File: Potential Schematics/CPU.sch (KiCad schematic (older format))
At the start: 0 parts

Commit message: Made the registers
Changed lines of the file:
@@
 $Descr A4 11693 8268
 encoding utf-8
-Sheet 2 22
+Sheet 2 449
 Title "CPU"
-Date ""
+Date "2018-09-14"
 Rev "1"
 Comp ""
@@
 	2100 4000 2800 4000
 Connection ~ 2100 3400
+$Sheet
+S 6450 2150 1350 1300
+U 5B9C0EA0
+F0 "Registers" 60
+F1 "Registers.sch" 60
+$EndSheet
 $EndSCHEMATC

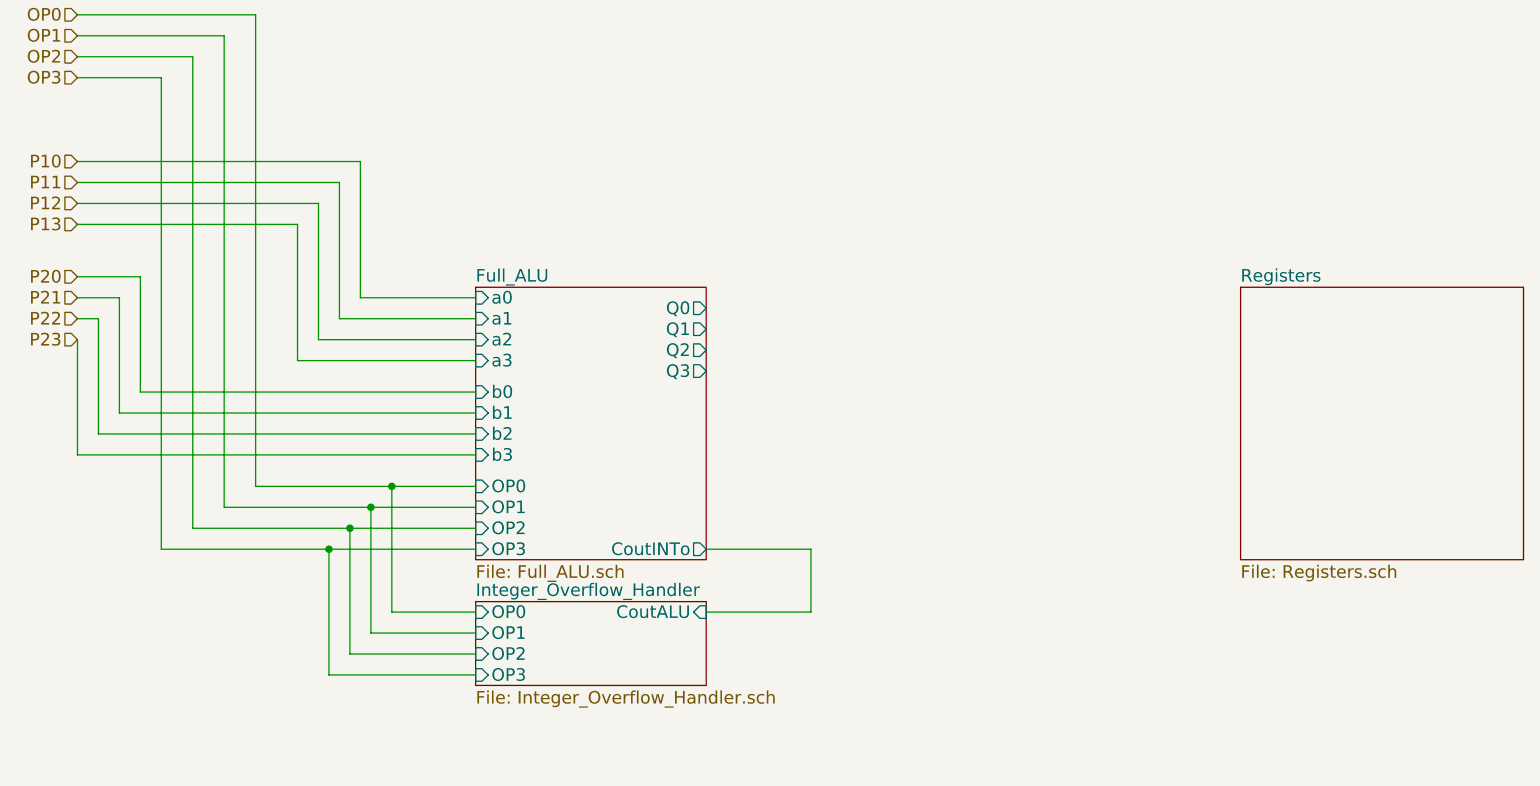
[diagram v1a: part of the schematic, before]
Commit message: Added Registers to Top Schematic
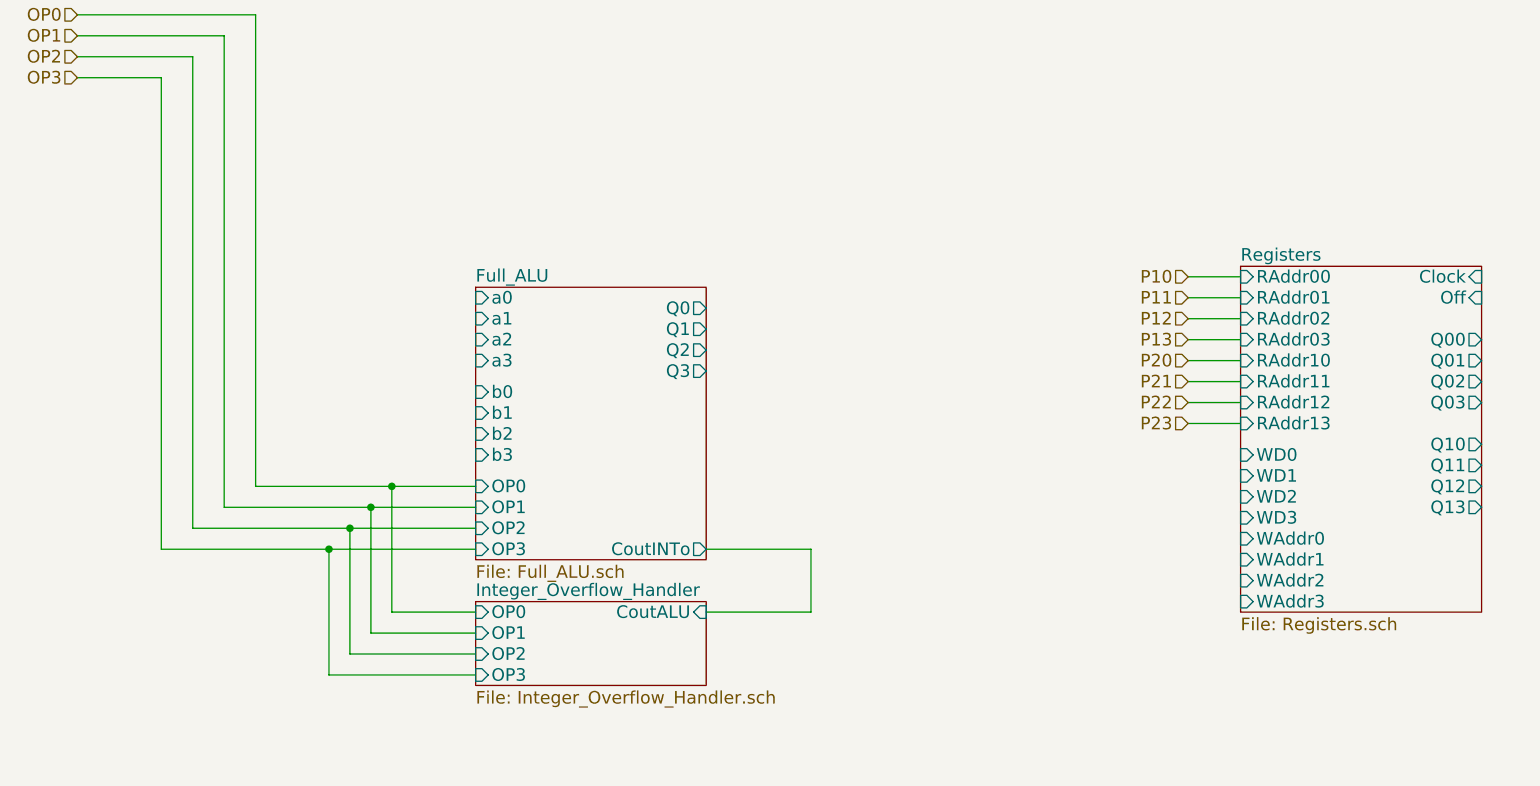
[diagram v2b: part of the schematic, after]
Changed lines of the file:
@@
 Text HLabel 900  1150 0    60   Input ~ 0
 OP3
-Text HLabel 900  1550 0    60   Input ~ 0
+Text HLabel 6200 2100 0    60   Input ~ 0
 P10
-Text HLabel 900  1650 0    60   Input ~ 0
+Text HLabel 6200 2200 0    60   Input ~ 0
 P11
-Text HLabel 900  1750 0    60   Input ~ 0
+Text HLabel 6200 2300 0    60   Input ~ 0
 P12
-Text HLabel 900  1850 0    60   Input ~ 0
+Text HLabel 6200 2400 0    60   Input ~ 0
 P13
-Text HLabel 900  2100 0    60   Input ~ 0
+Text HLabel 6200 2500 0    60   Input ~ 0
 P20
-Text HLabel 900  2200 0    60   Input ~ 0
+Text HLabel 6200 2600 0    60   Input ~ 0
 P21
-Text HLabel 900  2300 0    60   Input ~ 0
+Text HLabel 6200 2700 0    60   Input ~ 0
 P22
-Text HLabel 900  2400 0    60   Input ~ 0
+Text HLabel 6200 2800 0    60   Input ~ 0
 P23
 Text HLabel 900  4700 0    60   Input ~ 0
@@
 Wire Wire Line
 	1300 3400 2800 3400
-Wire Wire Line
-	900  1550 2250 1550
-Wire Wire Line
-	2250 1550 2250 2200
-Wire Wire Line
-	2250 2200 2800 2200
-Wire Wire Line
-	900  1650 2150 1650
-Wire Wire Line
-	2150 1650 2150 2300
-Wire Wire Line
-	2150 2300 2800 2300
-Wire Wire Line
-	2800 2400 2050 2400
-Wire Wire Line
-	2050 2400 2050 1750
-Wire Wire Line
-	2050 1750 900  1750
-Wire Wire Line
-	1950 2500 2800 2500
-Wire Wire Line
-	2800 2650 1200 2650
-Wire Wire Line
-	1200 2650 1200 2100
-Wire Wire Line
-	1200 2100 900  2100
-Wire Wire Line
-	900  2200 1100 2200
-Wire Wire Line
-	1100 2200 1100 2750
-Wire Wire Line
-	1100 2750 2800 2750
-Wire Wire Line
-	900  2300 1000 2300
-Wire Wire Line
-	1000 2300 1000 2850
-Wire Wire Line
-	1000 2850 2800 2850
-Wire Wire Line
-	900  2950 2800 2950
-Wire Wire Line
-	900  2400 900  2950
-Wire Wire Line
-	1950 2500 1950 1850
-Wire Wire Line
-	1950 1850 900  1850
 $Sheet
 S 2800 3650 1100 400
@@
 Connection ~ 2100 3400
 $Sheet
-S 6450 2150 1350 1300
+S 6450 2050 1150 1650
 U 5B9C0EA0
 F0 "Registers" 60
 F1 "Registers.sch" 60
+F2 "RAddr00" I L 6450 2100 60
+F3 "RAddr01" I L 6450 2200 60
+F4 "RAddr02" I L 6450 2300 60
+F5 "RAddr03" I L 6450 2400 60
+F6 "RAddr10" I L 6450 2500 60
+F7 "RAddr11" I L 6450 2600 60
+F8 "RAddr12" I L 6450 2700 60
+F9 "RAddr13" I L 6450 2800 60
+F10 "Clock" I R 7600 2100 60
+F11 "WD0" I L 6450 2950 60
+F12 "WD1" I L 6450 3050 60
+F13 "WD2" I L 6450 3150 60
+F14 "WD3" I L 6450 3250 60
+F15 "WAddr0" I L 6450 3350 60
+F16 "WAddr1" I L 6450 3450 60
+F17 "WAddr2" I L 6450 3550 60
+F18 "WAddr3" I L 6450 3650 60
+F19 "Q00" O R 7600 2400 60
+F20 "Q01" O R 7600 2500 60
+F21 "Q02" O R 7600 2600 60
+F22 "Q03" O R 7600 2700 60
+F23 "Q10" O R 7600 2900 60
+F24 "Q11" O R 7600 3000 60
+F25 "Q12" O R 7600 3100 60
+F26 "Q13" O R 7600 3200 60
+F27 "Off" I R 7600 2200 60
 $EndSheet
+Wire Wire Line
+	6200 2100 6450 2100
+Wire Wire Line
+	6200 2200 6450 2200
+Wire Wire Line
+	6200 2300 6450 2300
+Wire Wire Line
+	6200 2400 6450 2400
+Wire Wire Line
+	6200 2500 6450 2500
+Wire Wire Line
+	6200 2600 6450 2600
+Wire Wire Line
+	6200 2700 6450 2700
+Wire Wire Line
+	6450 2800 6200 2800
 $EndSCHEMATC

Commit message: Minor Changes
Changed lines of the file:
@@
 Text HLabel 6200 2800 0    60   Input ~ 0
 P23
-Text HLabel 900  4700 0    60   Input ~ 0
+Text HLabel 6200 3350 0    60   Input ~ 0
 P30
-Text HLabel 900  4800 0    60   Input ~ 0
+Text HLabel 6200 3450 0    60   Input ~ 0
 P31
-Text HLabel 900  4900 0    60   Input ~ 0
+Text HLabel 6200 3550 0    60   Input ~ 0
 P32
-Text HLabel 900  5000 0    60   Input ~ 0
+Text HLabel 6200 3650 0    60   Input ~ 0
 P33
 Wire Wire Line
@@
 Wire Wire Line
 	6450 2800 6200 2800
+Wire Wire Line
+	6200 3350 6450 3350
+Wire Wire Line
+	6450 3450 6200 3450
+Wire Wire Line
+	6200 3550 6450 3550
+Wire Wire Line
+	6200 3650 6450 3650
+Wire Wire Line
+	3900 2250 4850 2250
+Wire Wire Line
+	4850 2250 4850 2950
+Wire Wire Line
+	4850 2950 6450 2950
+Wire Wire Line
+	3900 2350 4750 2350
+Wire Wire Line
+	4750 2350 4750 3050
+Wire Wire Line
+	4750 3050 6450 3050
+Wire Wire Line
+	6450 3150 4650 3150
+Wire Wire Line
+	4650 3150 4650 2450
+Wire Wire Line
+	4650 2450 3900 2450
+Wire Wire Line
+	3900 2550 4550 2550
+Wire Wire Line
+	4550 2550 4550 3250
+Wire Wire Line
+	4550 3250 6450 3250
+Wire Wire Line
+	7600 2400 8500 2400
+Wire Wire Line
+	8500 2400 8500 1650
+Wire Wire Line
+	8500 1650 2700 1650
+Wire Wire Line
+	2700 1650 2700 2200
+Wire Wire Line
+	2700 2200 2800 2200
+Wire Wire Line
+	7600 2500 8600 2500
+Wire Wire Line
+	8600 2500 8600 1550
+Wire Wire Line
+	8600 1550 2600 1550
+Wire Wire Line
+	2600 1550 2600 2300
+Wire Wire Line
+	2600 2300 2800 2300
+Wire Wire Line
+	2800 2400 2500 2400
+Wire Wire Line
+	2500 2400 2500 1450
+Wire Wire Line
+	2500 1450 8700 1450
+Wire Wire Line
+	8700 1450 8700 2600
+Wire Wire Line
+	8700 2600 7600 2600
+Wire Wire Line
+	7600 2700 8800 2700
+Wire Wire Line
+	8800 2700 8800 1350
+Wire Wire Line
+	8800 1350 2400 1350
+Wire Wire Line
+	2400 1350 2400 2500
+Wire Wire Line
+	2400 2500 2800 2500
 $EndSCHEMATC

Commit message: Adding Multiply Devide
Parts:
- added U?: 74LS08, symbol 74xx:74LS08
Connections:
- net labels added: Clock
- wire segments 67 -> 100
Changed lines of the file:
@@
-EESchema Schematic File Version 2
-LIBS:power
-LIBS:device
-LIBS:switches
-LIBS:relays
-LIBS:motors
-LIBS:transistors
-LIBS:conn
-LIBS:linear
-LIBS:regul
-LIBS:74xx
-LIBS:cmos4000
-LIBS:adc-dac
-LIBS:memory
-LIBS:xilinx
-LIBS:microcontrollers
-LIBS:dsp
-LIBS:microchip
-LIBS:analog_switches
-LIBS:motorola
-LIBS:texas
-LIBS:intel
-LIBS:audio
-LIBS:interface
-LIBS:digital-audio
-LIBS:philips
-LIBS:display
-LIBS:cypress
-LIBS:siliconi
-LIBS:opto
-LIBS:atmel
-LIBS:contrib
-LIBS:valves
+EESchema Schematic File Version 4
 LIBS:4-bit_processor-cache
-EELAYER 25 0
+EELAYER 26 0
 EELAYER END
 $Descr A4 11693 8268
 encoding utf-8
-Sheet 2 449
+Sheet 2 451
 Title "CPU"
 Date "2018-09-14"
@@
 	1750 850  1750 3100
 Wire Wire Line
-	1750 3100 2800 3100
+	1750 3100 2400 3100
 Wire Wire Line
 	900  950  1600 950
@@
 	1600 950  1600 3200
 Wire Wire Line
-	1600 3200 2800 3200
-Wire Wire Line
-	2800 3300 1450 3300
+	1600 3200 2300 3200
+Wire Wire Line
+	2800 3300 2200 3300
 Wire Wire Line
 	1450 3300 1450 1050
@@
 	1300 1150 1300 3400
 Wire Wire Line
-	1300 3400 2800 3400
+	1300 3400 2100 3400
 $Sheet
 S 2800 3650 1100 400
@@
 Wire Wire Line
 	2400 2500 2800 2500
+Wire Wire Line
+	2400 3100 2800 3100
+Wire Wire Line
+	2300 3200 2800 3200
+Wire Wire Line
+	2200 3300 1450 3300
+Wire Wire Line
+	2100 3400 2800 3400
+$Comp
+L 74xx:74LS08 U?
+U 1 1 5BA7B2CE
+P 2450 650
+F 0 "U?" H 2550 450 50  0000 C CNN
+F 1 "74LS08" H 2300 450 50  0000 C CNN
+F 2 "" H 2450 650 50  0001 C CNN
+F 3 "http://www.ti.com/lit/gpn/sn74LS08" H 2450 650 50  0001 C CNN
+	1    2450 650
+	1    0    0    -1
+$EndComp
+Wire Wire Line
+	7700 2200 7600 2200
+Text HLabel 10100 2100 2    50   Input ~ 0
+Clock
+Wire Wire Line
+	7600 2100 10100 2100
+Wire Wire Line
+	7600 2900 8900 2900
+Wire Wire Line
+	8900 2900 8900 1250
+Wire Wire Line
+	8900 1250 2300 1250
+Wire Wire Line
+	2300 1250 2300 2650
+Wire Wire Line
+	2300 2650 2800 2650
+Wire Wire Line
+	1750 850  1750 550
+Wire Wire Line
+	1750 550  2150 550
+Connection ~ 1750 850
+Wire Wire Line
+	1300 1150 1800 1150
+Wire Wire Line
+	1800 1150 1800 750
+Wire Wire Line
+	1800 750  2150 750
+Connection ~ 1300 1150
+Wire Wire Line
+	2750 650  7700 650
+Wire Wire Line
+	7700 650  7700 2200
+Wire Wire Line
+	2800 2750 2200 2750
+Wire Wire Line
+	2200 2750 2200 1150
+Wire Wire Line
+	2200 1150 9000 1150
+Wire Wire Line
+	9000 1150 9000 3000
+Wire Wire Line
+	9000 3000 7600 3000
+Wire Wire Line
+	7600 3100 9100 3100
+Wire Wire Line
+	9100 3100 9100 1050
+Wire Wire Line
+	9100 1050 2100 1050
+Wire Wire Line
+	2100 1050 2100 2850
+Wire Wire Line
+	2100 2850 2800 2850
+Wire Wire Line
+	2800 2950 2000 2950
+Wire Wire Line
+	2000 2950 2000 950
+Wire Wire Line
+	2000 950  9200 950
+Wire Wire Line
+	9200 950  9200 3200
+Wire Wire Line
+	9200 3200 7600 3200
+$Sheet
+S 2800 4600 1100 1150
+U 5BAA33A0
+F0 "Multiply_Devide_ALU" 50
+F1 "Mult_Devide.sch" 50
+$EndSheet
 $EndSCHEMATC

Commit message: Finished PCB
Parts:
- removed U?: 74LS08, symbol 74xx:74LS08
- added U1: 74LS08, Daniel_Kopp:DIP-14_300_ELL, symbol 4-bit_processor-rescue:74LS08
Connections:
- wire segments 100 -> 101
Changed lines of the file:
@@
 $Descr A4 11693 8268
 encoding utf-8
-Sheet 2 451
+Sheet 2 456
 Title "CPU"
 Date "2018-09-14"
@@
 Wire Wire Line
 	2100 3400 2800 3400
-$Comp
-L 74xx:74LS08 U?
-U 1 1 5BA7B2CE
-P 2450 650
-F 0 "U?" H 2550 450 50  0000 C CNN
-F 1 "74LS08" H 2300 450 50  0000 C CNN
-F 2 "" H 2450 650 50  0001 C CNN
-F 3 "http://www.ti.com/lit/gpn/sn74LS08" H 2450 650 50  0001 C CNN
-	1    2450 650
-	1    0    0    -1
-$EndComp
 Wire Wire Line
 	7700 2200 7600 2200
@@
 	2300 2650 2800 2650
 Wire Wire Line
-	1750 850  1750 550
-Wire Wire Line
-	1750 550  2150 550
+	1750 850  1750 600
+Wire Wire Line
+	1750 600  2150 600
 Connection ~ 1750 850
 Wire Wire Line
 	1300 1150 1800 1150
 Wire Wire Line
-	1800 1150 1800 750
-Wire Wire Line
-	1800 750  2150 750
+	1800 1150 1800 800
+Wire Wire Line
+	1800 800  2150 800
 Connection ~ 1300 1150
-Wire Wire Line
-	2750 650  7700 650
 Wire Wire Line
 	7700 650  7700 2200
@@
 F1 "Mult_Devide.sch" 50
 $EndSheet
+$Comp
+L 4-bit_processor-rescue:74LS08 U1
+U 1 1 5BA57CCF
+P 2750 700
+F 0 "U1" H 3150 500 50  0000 C CNN
+F 1 "74LS08" H 3300 600 50  0000 C CNN
+F 2 "Daniel_Kopp:DIP-14_300_ELL" H 2750 700 50  0001 C CNN
+F 3 "" H 2750 700 50  0001 C CNN
+	1    2750 700
+	1    0    0    -1
+$EndComp
+Wire Wire Line
+	3350 650  7700 650
+Wire Wire Line
+	3350 650  3350 700
 $EndSCHEMATC

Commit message: Made Multiplier
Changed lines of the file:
@@
 $Descr A4 11693 8268
 encoding utf-8
-Sheet 2 458
+Sheet 2 467
 Title "CPU"
 Date "2018-09-14"
@@
 S 2800 4600 1100 1150
 U 5BAA33A0
-F0 "Multiply_Devide_ALU" 50
-F1 "Mult_Devide.sch" 50
+F0 "Multiply_Divide_ALU" 50
+F1 "Mult_Divide.sch" 50
 $EndSheet
 $Comp
@@
 Wire Wire Line
 	3350 650  3350 700
+$Sheet
+S 2800 6050 1100 400
+U 5BB0D9CD
+F0 "Multiplicitive_Overflow" 60
+F1 "Integer_Overflow_Handler.sch" 60
+F2 "OP0" I L 2800 6100 60
+F3 "OP1" I L 2800 6200 60
+F4 "OP2" I L 2800 6300 60
+F5 "OP3" I L 2800 6400 60
+F6 "CoutALU" I R 3900 6100 60
+$EndSheet
 $EndSCHEMATC

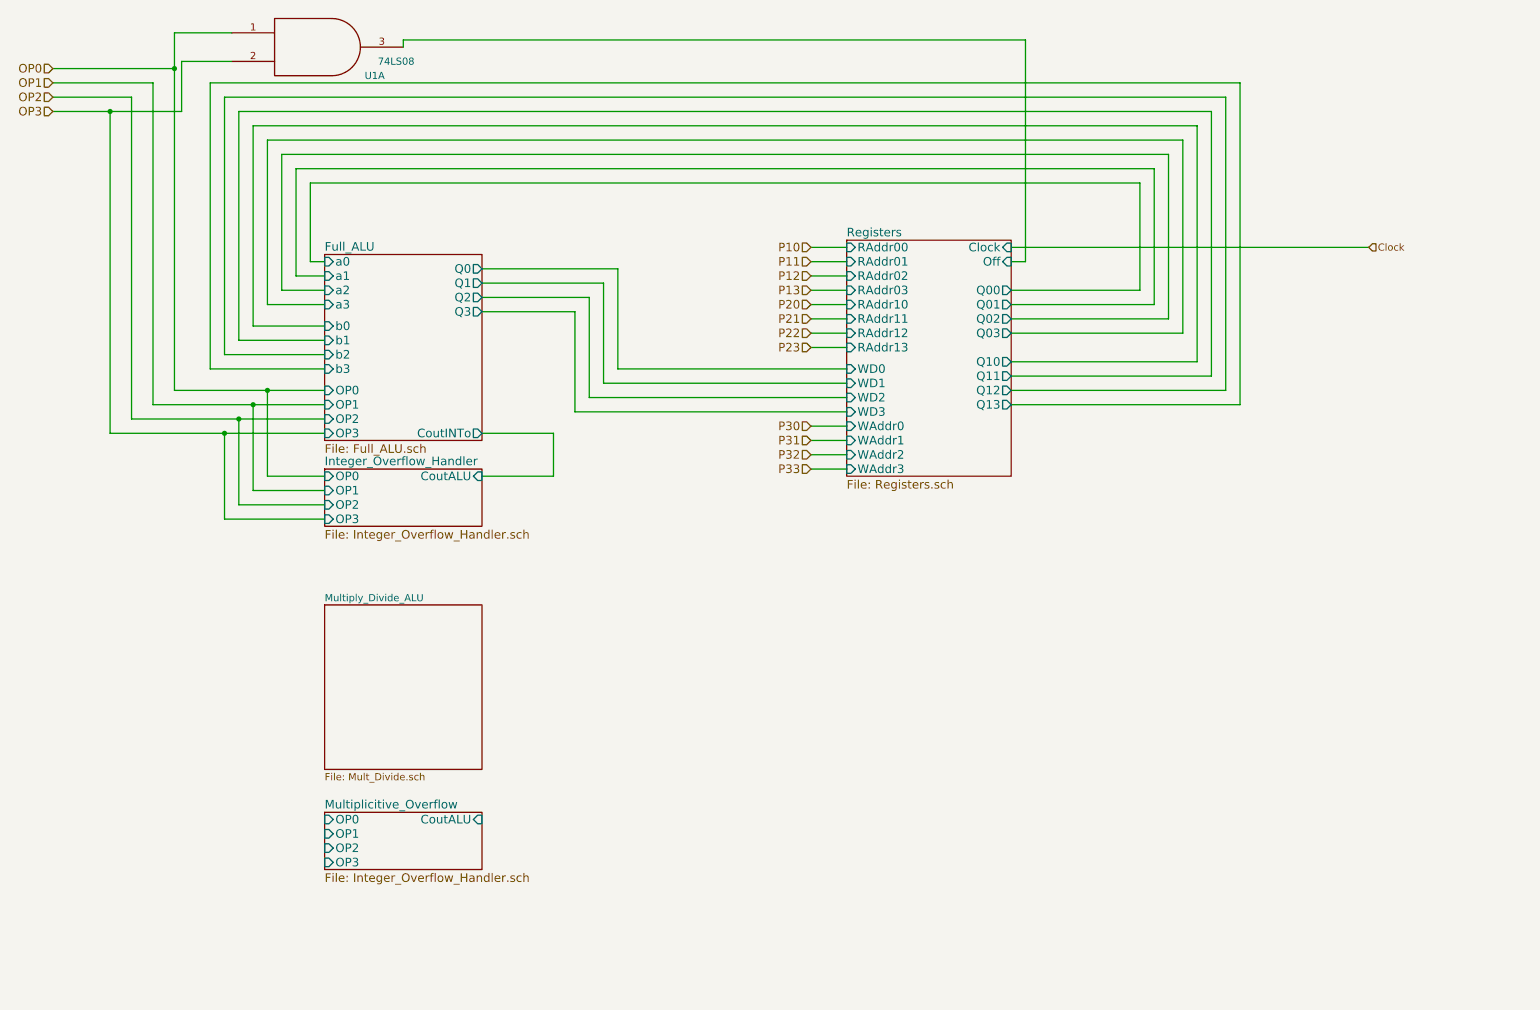
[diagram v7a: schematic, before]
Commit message: Updated overview of Schematic
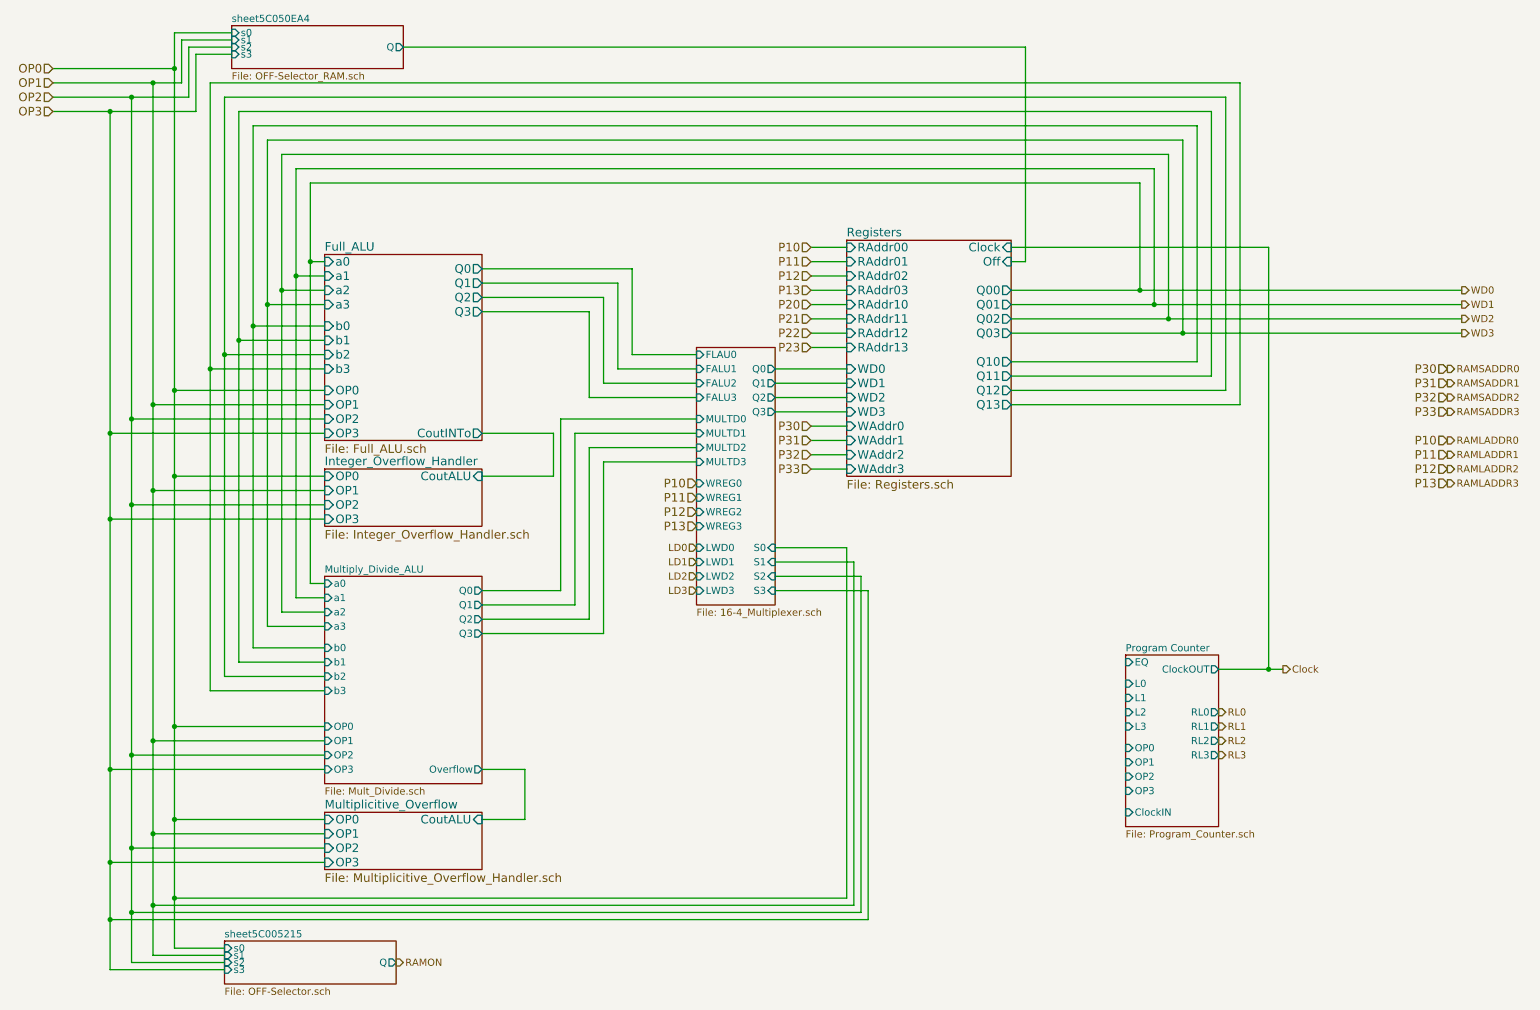
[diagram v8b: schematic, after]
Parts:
- removed U1: 74LS08, Daniel_Kopp:DIP-14_300_ELL, symbol 4-bit_processor-rescue:74LS08
